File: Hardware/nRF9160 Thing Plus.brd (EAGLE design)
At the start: 22.9 x 58.4 mm, 128 parts, among them J1 USB Female C, J10 QWIIC_RIGHT_ANGLE, J2 CON-HEADER-1X12-MALE-PIN, J3 CON-HEADER-1X16-MALE-PIN, J4 CON-1909763-1, J6 CON-SIM-104224-0820, J7 CON-1909763-1, J8 CON-FTSH-105-XX-X-DV, Q1 MOSFET-P-SC89, Q2 MOSFET-DUAL-COMP-SOT563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

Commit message: Updated BOM
replaced SW1 and SW2 to new taller momentary switch
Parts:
- SW1, SW2: value MOMENTARY-SWITCH-SPST-SMD-4.6X2.8MM -> (none)

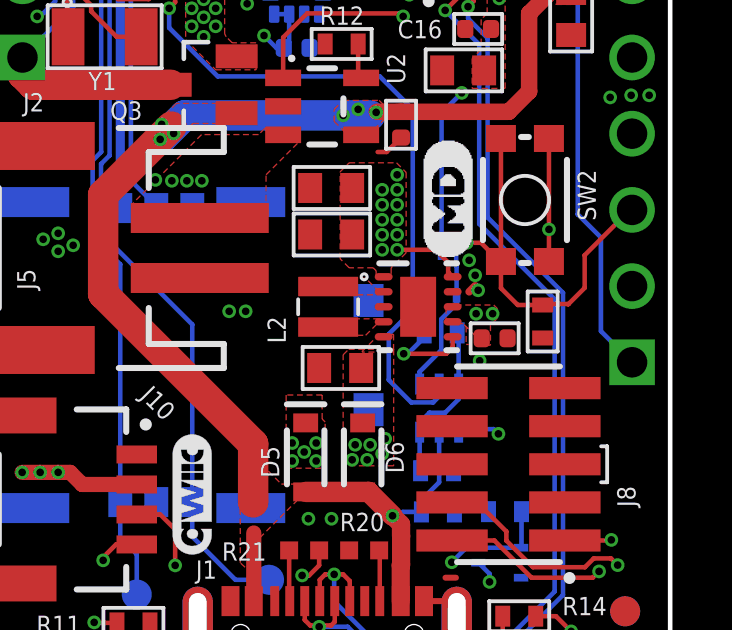
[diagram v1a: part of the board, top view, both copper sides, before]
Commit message: Making adjustments to power supply
Changed:
* Pin 7 of U3 grounded.
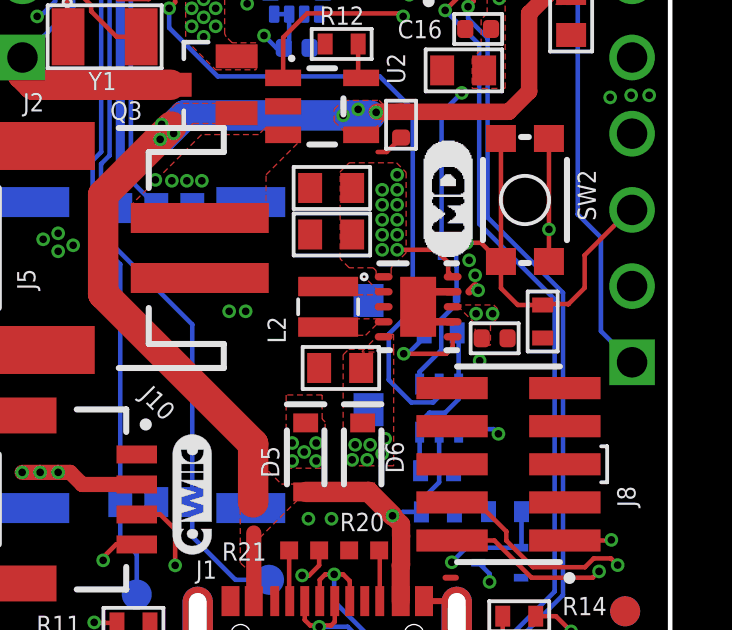
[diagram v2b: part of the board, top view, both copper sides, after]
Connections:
- net GND: now also U3.7
- net VSYS: no longer U3.7
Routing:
- net GND: track 37.2 -> 39.6 mm
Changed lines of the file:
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@@
 <drawing>
 <settings>
-<setting alwaysvectorfont="yes"/>
+<setting alwaysvectorfont="no"/>
 <setting keepoldvectorfont="yes"/>
 <setting verticaltext="up"/>
 </settings>
-<grid distance="0.05" unitdist="inch" unit="inch" style="lines" multiple="1" display="yes" altdistance="0.005" altunitdist="inch" altunit="inch"/>
+<grid distance="0.1" unitdist="mm" unit="mm" style="lines" multiple="1" display="yes" altdistance="0.005" altunitdist="inch" altunit="inch"/>
 <layers>
 <layer number="1" name="Top" color="4" fill="1" visible="yes" active="yes"/>
-<layer number="16" name="Bottom" color="1" fill="1" visible="yes" active="yes"/>
+<layer number="16" name="Bottom" color="1" fill="1" visible="no" active="yes"/>
 <layer number="17" name="Pads" color="2" fill="1" visible="yes" active="yes"/>
 <layer number="18" name="Vias" color="2" fill="1" visible="yes" active="yes"/>
@@
 <layer number="20" name="Dimension" color="24" fill="1" visible="yes" active="yes"/>
 <layer number="21" name="tPlace" color="16" fill="1" visible="yes" active="yes"/>
-<layer number="22" name="bPlace" color="14" fill="1" visible="yes" active="yes"/>
+<layer number="22" name="bPlace" color="14" fill="1" visible="no" active="yes"/>
 <layer number="23" name="tOrigins" color="15" fill="1" visible="yes" active="yes"/>
-<layer number="24" name="bOrigins" color="15" fill="1" visible="yes" active="yes"/>
-<layer number="25" name="tNames" color="7" fill="1" visible="no" active="yes"/>
+<layer number="24" name="bOrigins" color="15" fill="1" visible="no" active="yes"/>
+<layer number="25" name="tNames" color="7" fill="1" visible="yes" active="yes"/>
 <layer number="26" name="bNames" color="7" fill="1" visible="no" active="yes"/>
 <layer number="27" name="tValues" color="7" fill="1" visible="no" active="yes"/>
@@
 <layer number="37" name="tTest" color="7" fill="1" visible="no" active="yes"/>
 <layer number="38" name="bTest" color="7" fill="1" visible="no" active="yes"/>
-<layer number="39" name="tKeepout" color="4" fill="11" visible="no" active="yes"/>
+<layer number="39" name="tKeepout" color="4" fill="11" visible="yes" active="yes"/>
 <layer number="40" name="bKeepout" color="1" fill="11" visible="no" active="yes"/>
-<layer number="41" name="tRestrict" color="4" fill="10" visible="no" active="yes"/>
+<layer number="41" name="tRestrict" color="4" fill="10" visible="yes" active="yes"/>
 <layer number="42" name="bRestrict" color="1" fill="10" visible="no" active="yes"/>
 <layer number="43" name="vRestrict" color="2" fill="10" visible="no" active="yes"/>
 <layer number="44" name="Drills" color="7" fill="1" visible="no" active="yes"/>
-<layer number="45" name="Holes" color="7" fill="1" visible="yes" active="yes"/>
+<layer number="45" name="Holes" color="7" fill="1" visible="no" active="yes"/>
 <layer number="46" name="Milling" color="3" fill="1" visible="no" active="yes"/>
 <layer number="47" name="Measures" color="7" fill="1" visible="no" active="yes"/>
@@
 <wire x1="15.748" y1="5.925" x2="15.748" y2="5.435" width="0.2" layer="1"/>
 <wire x1="15.72" y1="6.79" x2="15.37" y2="6.79" width="0.2" layer="1"/>
+<contactref element="U3" pad="7"/>
+<wire x1="15.61" y1="16.32" x2="14.68" y2="16.32" width="0.254" layer="1"/>
+<wire x1="14.68" y1="16.32" x2="14.6" y2="16.4" width="0.254" layer="1"/>
+<wire x1="15.61" y1="15.320003125" x2="14.959996875" y2="15.320003125" width="0.254" layer="1"/>
+<wire x1="14.959996875" y1="15.320003125" x2="14.46" y2="15.82" width="0.254" layer="1"/>
 </signal>
 <signal name="+3V3">
@@
 <contactref element="C6" pad="1"/>
 <contactref element="U3" pad="5"/>
-<contactref element="U3" pad="7"/>
 <contactref element="U3" pad="8"/>
 <polygon width="0.1524" layer="1" thermals="no">
@@
 <via x="13.26" y="10.92" extent="1-16" drill="0.254"/>
 <polygon width="0.1524" layer="1" thermals="no">
-<vertex x="16.06" y="15.165834375"/>
-<vertex x="16.06" y="14.565834375"/>
+<vertex x="16.46" y="14.796603125"/>
+<vertex x="16.46" y="14.565834375"/>
 <vertex x="16.71" y="14.565834375"/>
 </polygon>
@@
 <vertex x="16.39" y="14.54"/>
 <vertex x="16.36" y="14.57"/>
-<vertex x="16.36" y="14.86"/>
-<vertex x="15.96" y="15.26"/>
-<vertex x="15.4" y="15.26"/>
-<vertex x="15.39" y="15.27"/>
+<vertex x="16.36" y="15.26"/>
+<vertex x="15.85" y="15.77"/>
+<vertex x="15.39" y="15.77"/>
 <vertex x="15.39" y="15.88"/>
 <vertex x="16.98" y="15.88"/>
